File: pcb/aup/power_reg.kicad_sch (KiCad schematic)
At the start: 53 parts, among them Q2 AO3400A, Q3 AO3401A, U5 TPS563257DRLR, U6 ISL80103IRAJZ-TK, U7 TPS563257DRLR, U8 TPS563257DRLR, U9 TPS563257DRLR

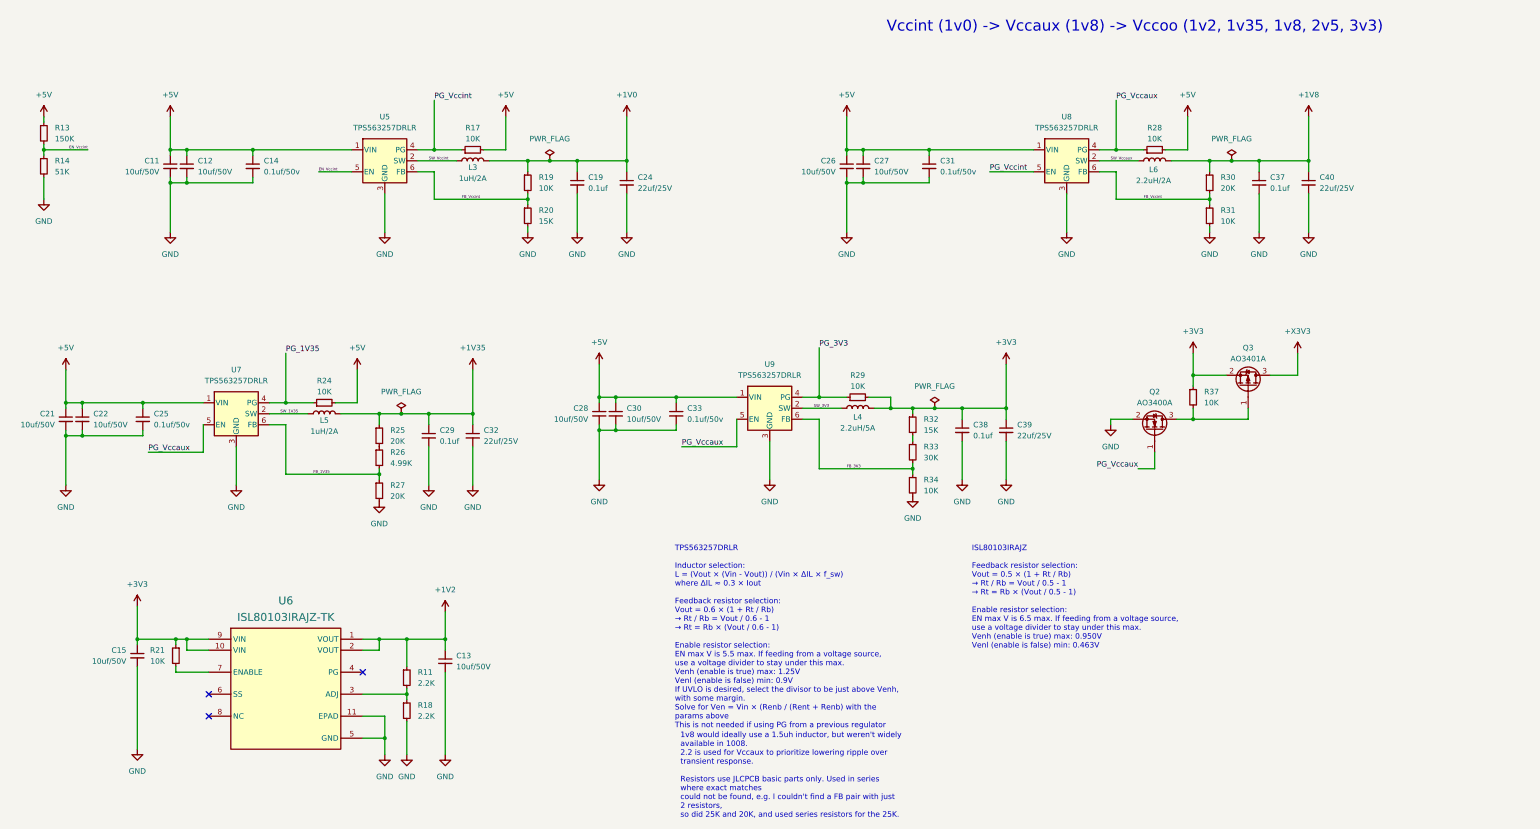
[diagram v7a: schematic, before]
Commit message: GTP 1.0 and 1.2 LDOs routed
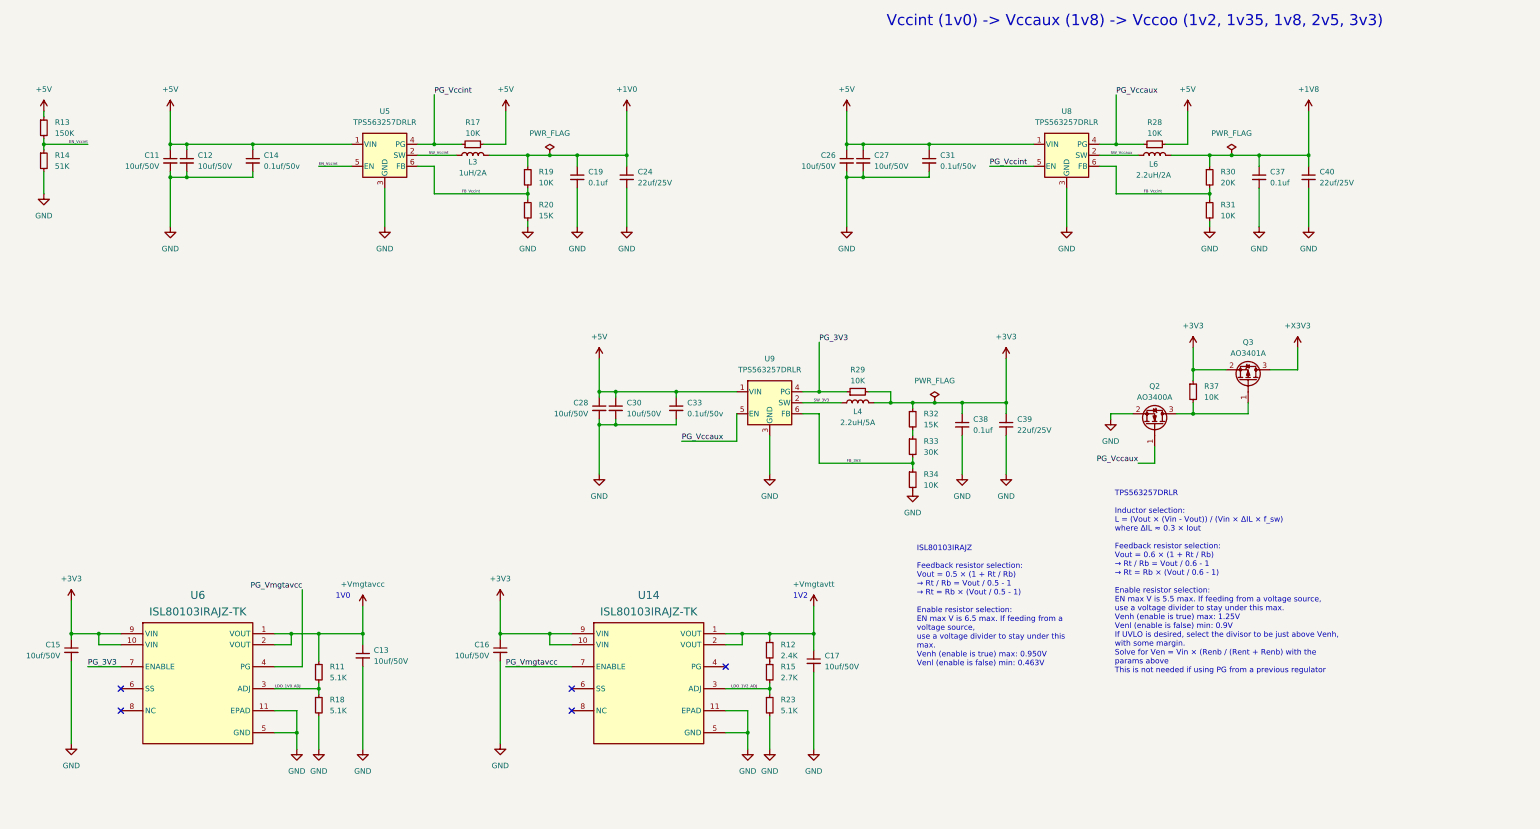
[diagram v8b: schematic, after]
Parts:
- removed C21, C22: 10uf/50V, Capacitor_SMD:C_0805_2012Metric, symbol !Misc:C_10uf_0805
- removed C25: 0.1uf/50v, Capacitor_SMD:C_0603_1608Metric, symbol !Misc:C_0.1uf_0603
- removed C29: 0.1uf, Capacitor_SMD:C_0402_1005Metric, symbol !Misc:C_0.1uf_0402
- removed C32: 22uf/25V, Capacitor_SMD:C_0805_2012Metric, symbol !Misc:C_22uf_0805
- removed L5: 1uH/2A, Inductor_SMD:L_1008_2520Metric, symbol !Misc:L_1uh_3A
- removed R21, R24: 10K, Resistor_SMD:R_0603_1608Metric, symbol !Misc:R_10K_0603
- removed R25, R27: 20K, Resistor_SMD:R_0603_1608Metric, symbol !Misc:R_20K_0603
- removed R26: 4.99K, Resistor_SMD:R_0603_1608Metric, symbol !Misc:R_4.99K_0603
- removed U7: TPS563257DRLR, !Misc:SOT6_DRL_TEX, symbol !Misc:TPS563257DRLR
- added C16, C17: 10uf/50V, Capacitor_SMD:C_0805_2012Metric, symbol !Misc:C_10uf_0805
- added R12: 2.4K, Resistor_SMD:R_0603_1608Metric, symbol !Misc:R_2.4K_0603
- added R15: 2.7K, Resistor_SMD:R_0603_1608Metric, symbol !Misc:R_2.7K_0603
- added R23: 5.1K, Resistor_SMD:R_0603_1608Metric, symbol !Misc:R_5.1K_0603
- added U14: ISL80103IRAJZ-TK, !Misc:DFN10_3X3_INR, symbol !Misc:ISL80103IRAJZ-TK
- R11, R18: value 2.2K -> 5.1K; symbol !Misc:R_2.2K_0603 -> !Misc:R_5.1K_0603; Digi-Key Part Number 118-CR0603-FX-2201ELFCT-ND -> CR0603-FX-5101ELFCT-ND; LCSC Part # C25879 -> C23186
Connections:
- net +3V3: now also C16.1, U14.10 (VIN), U14.9 (VIN)
- net GND: now also C16.2, C17.2, R23.2, U14.11 (EPAD), U14.5 (GND)
- net PG_3V3: now also U6.7 (ENABLE)
- net LDO_1V0_ADJ: now reaches R11.2, R18.1, U6.3 (ADJ)
- net PG_Vmgtavcc: now reaches U6.4 (PG)
- net PG_Vmgtavcc: now also U14.7 (ENABLE)
- net +1V2 renamed +Vmgtavcc
- new net: R12.2, R15.1
- new net +Vmgtavtt: C17.1, R12.1, U14.1 (VOUT), U14.2 (VOUT)
- new net LDO_1V2_ADJ: R15.2, R23.1, U14.3 (ADJ)
- no-connect marks 3 -> 5
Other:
- note added: "1V0"
- note added: "1V2"
- moved on the sheet: C11, C12, C13, C14, C15, C19, C24, C26, C27, C28, C30, C31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
